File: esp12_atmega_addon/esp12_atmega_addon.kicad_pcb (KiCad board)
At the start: 2 copper layers, 16 x 24 mm, 11 parts, among them U1 ESP-12E, U2 ATMEGA328P-MU

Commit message: Fixed DRC violations and changed the pinout a little bit
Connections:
- U1 pad 10: MISO -> PB1
- U1 pad 11: PB1 -> MISO
- U2 pad 33: GND -> (no net)
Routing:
- net PB1: track 2.87 -> 4.38 mm
- net RXD: track 13.4 -> 14.8 mm
- net MISO: track 6.32 -> 5.04 mm
- net ADC: track 11.4 -> 12.5 mm
- net TXD: track 15.1 -> 16.2 mm
- net Net-(U1-Pad4): track 5.04 -> 6.07 mm
- net Net-(U1-Pad5): track 4.45 -> 5.45 mm
- net GND: track 85.6 -> 86.6 mm
- net A2: track 6.20 -> 7.20 mm
- net A1: track 6.11 -> 7.11 mm
- net A0: track 8.60 -> 9.60 mm
- net A4: track 9.54 -> 10.5 mm
- net RST: track 26.2 -> 27.1 mm
- net Net-(U1-Pad7): track 7.11 -> 7.91 mm
- net INT: track 6.22 -> 7.00 mm
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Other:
- board text added: "ATMega328P mod for ZeroPhone by CRImier, v1.0"
- board text added: "ATMega328P mod for ZeroPhone, v1.0"
- board text removed: "ATMega328P mod"

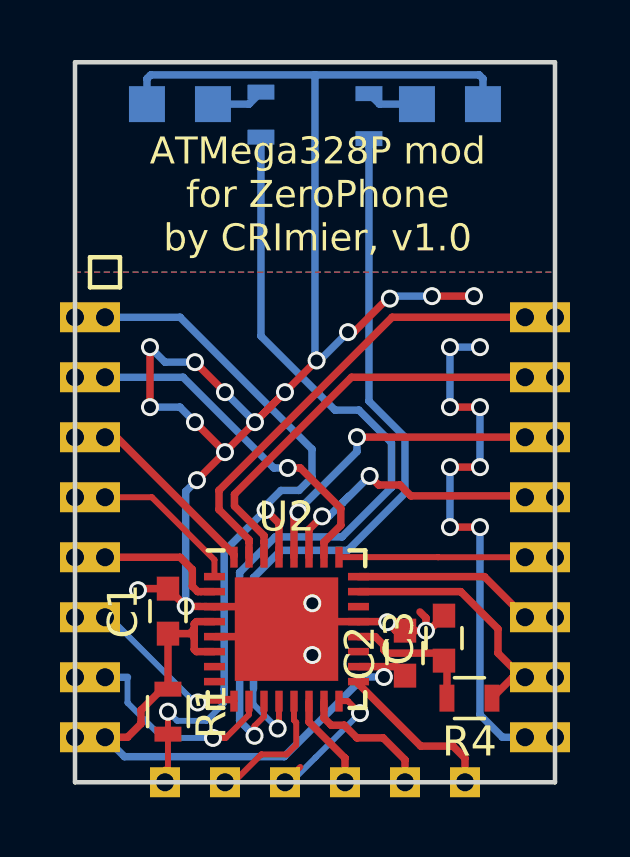
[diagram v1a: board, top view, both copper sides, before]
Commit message: Tying XTAL pins to ground
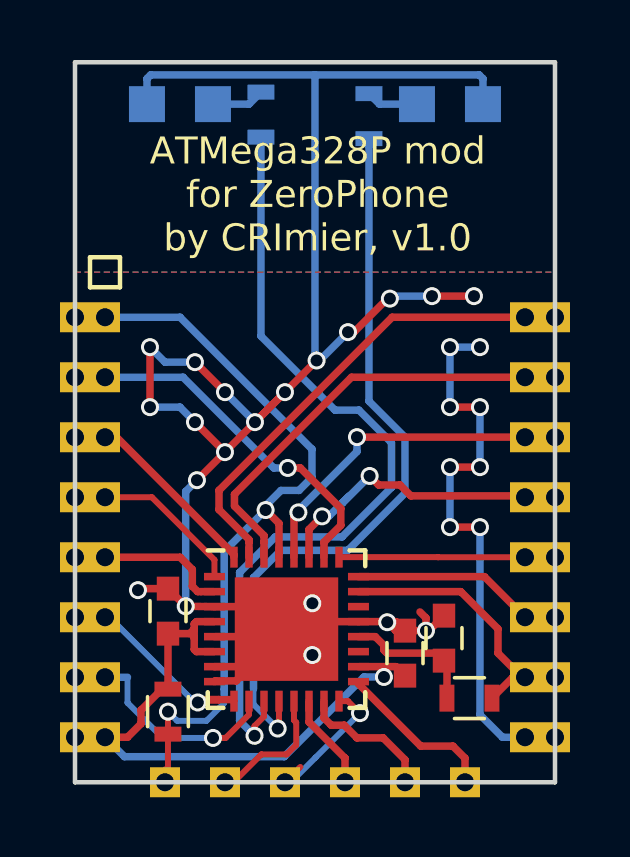
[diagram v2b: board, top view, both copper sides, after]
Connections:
- U2 pad 33: (no net) -> GND
- U2 pad 7: (no net) -> GND
- U2 pad 8: (no net) -> GND
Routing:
- net GND: track 86.6 -> 90.2 mm
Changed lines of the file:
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@@
 (kicad_pcb (version 4) (host pcbnew 4.0.7)
   (general
-    (links 58)
-    (no_connects 0)
+    (links 64)
+    (no_connects 1)
     (area 139.8011 91.549999 157.2011 117.85)
     (thickness 1.6)
     (drawings 2)
-    (tracks 308)
+    (tracks 315)
     (zones 0)
     (modules 11)
@@
     (45 Margin user)
     (46 B.CrtYd user hide)
-    (47 F.CrtYd user)
+    (47 F.CrtYd user hide)
     (48 B.Fab user hide)
     (49 F.Fab user hide)
@@
     (tags "capacitor 0603")
     (attr smd)
-    (fp_text reference C1 (at 0 -1.5 90) (layer F.SilkS)
+    (fp_text reference C1 (at 0 -1.5 90) (layer F.SilkS) hide
       (effects (font (size 1 1) (thickness 0.15)))
     )
@@
     (tags "capacitor 0603")
     (attr smd)
-    (fp_text reference C2 (at 0 -1.5 90) (layer F.SilkS)
+    (fp_text reference C2 (at 0 -1.5 90) (layer F.SilkS) hide
       (effects (font (size 1 1) (thickness 0.15)))
     )
@@
     (tags "capacitor 0603")
     (attr smd)
-    (fp_text reference C3 (at 0 -1.5 90) (layer F.SilkS)
+    (fp_text reference C3 (at 0 -1.5 90) (layer F.SilkS) hide
       (effects (font (size 1 1) (thickness 0.15)))
     )
@@
     (tags "QFN 0.5")
     (attr smd)
-    (fp_text reference U2 (at 0 -3.75) (layer F.SilkS)
+    (fp_text reference U2 (at 0 -3.75) (layer F.SilkS) hide
       (effects (font (size 1 1) (thickness 0.15)))
     )
@@
     (pad 6 smd rect (at -2.4 0.75) (size 0.7 0.25) (layers F.Cu F.Paste F.Mask)
       (net 5 +3V3))
-    (pad 7 smd rect (at -2.4 1.25) (size 0.7 0.25) (layers F.Cu F.Paste F.Mask))
-    (pad 8 smd rect (at -2.4 1.75) (size 0.7 0.25) (layers F.Cu F.Paste F.Mask))
+    (pad 7 smd rect (at -2.4 1.25) (size 0.7 0.25) (layers F.Cu F.Paste F.Mask)
+      (net 6 GND))
+    (pad 8 smd rect (at -2.4 1.75) (size 0.7 0.25) (layers F.Cu F.Paste F.Mask)
+      (net 6 GND))
     (pad 9 smd rect (at -1.75 2.4 90) (size 0.7 0.25) (layers F.Cu F.Paste F.Mask)
       (net 3 "Net-(U1-Pad6)"))
@@
       (net 9 INT))
     (pad 33 smd rect (at 0.8625 0.8625) (size 1.725 1.725) (layers F.Cu F.Paste F.Mask)
-      (solder_paste_margin_ratio -0.2))
+      (net 6 GND) (solder_paste_margin_ratio -0.2))
     (pad 33 smd rect (at 0.8625 -0.8625) (size 1.725 1.725) (layers F.Cu F.Paste F.Mask)
-      (solder_paste_margin_ratio -0.2))
+      (net 6 GND) (solder_paste_margin_ratio -0.2))
     (pad 33 smd rect (at -0.8625 0.8625) (size 1.725 1.725) (layers F.Cu F.Paste F.Mask)
-      (solder_paste_margin_ratio -0.2))
+      (net 6 GND) (solder_paste_margin_ratio -0.2))
     (pad 33 smd rect (at -0.8625 -0.8625) (size 1.725 1.725) (layers F.Cu F.Paste F.Mask)
-      (solder_paste_margin_ratio -0.2))
+      (net 6 GND) (solder_paste_margin_ratio -0.2))
     (model Housings_DFN_QFN.3dshapes/QFN-32-1EP_5x5mm_Pitch0.5mm.wrl
       (at (xyz 0 0 0))
@@
     (tags "resistor 0603")
     (attr smd)
-    (fp_text reference R1 (at 0 -1.45 270) (layer F.SilkS)
+    (fp_text reference R1 (at 0 -1.45 270) (layer F.SilkS) hide
       (effects (font (size 1 1) (thickness 0.15)))
     )
@@
     (tags "resistor 0603")
     (attr smd)
-    (fp_text reference R4 (at 0 -1.45 180) (layer F.SilkS)
+    (fp_text reference R4 (at 0 -1.45 180) (layer F.SilkS) hide
       (effects (font (size 1 1) (thickness 0.15)))
     )
@@
     )
   )
-  (gr_text "ATMega328P mod\nfor ZeroPhone\nby CRImier, v1.0" (at 148.59 97.409 360) (layer F.SilkS)
+  (gr_text "ATMega328P mod\nfor ZeroPhone\nby CRImier, v1.0" (at 148.59 97.409) (layer F.SilkS)
     (effects (font (size 0.9 0.9) (thickness 0.17)))
   )
@@
   (segment (start 144.474999 112.574999) (end 144.55 112.65) (width 0.25) (layer F.Cu) (net 5))
   (segment (start 144.55 112.65) (end 145.15 112.65) (width 0.25) (layer F.Cu) (net 5))
+  (segment (start 145.876641 113.624999) (end 145.175001 113.624999) (width 0.25) (layer F.Cu) (net 6))
+  (segment (start 145.175001 113.624999) (end 145.15 113.65) (width 0.25) (layer F.Cu) (net 6))
+  (segment (start 146.6875 112.7625) (end 146.6875 112.81414) (width 0.25) (layer F.Cu) (net 6))
+  (segment (start 146.6875 112.81414) (end 145.876641 113.624999) (width 0.25) (layer F.Cu) (net 6))
+  (segment (start 145.15 113.15) (end 146.3 113.15) (width 0.25) (layer F.Cu) (net 6))
+  (segment (start 146.3 113.15) (end 146.6875 112.7625) (width 0.25) (layer F.Cu) (net 6))
+  (segment (start 145.15084 113.15084) (end 145.15 113.15) (width 0.25) (layer F.Cu) (net 6))
   (segment (start 145.15 112.15) (end 146.075 112.15) (width 0.25) (layer F.Cu) (net 6))
   (via (at 150.996699 100.883068) (size 0.6) (drill 0.4) (layers F.Cu B.Cu) (net 6))
